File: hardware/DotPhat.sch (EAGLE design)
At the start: 44 parts, among them CN1 1X4-BIG, IC1 CAT24M010TS, J2 RASPBERRYPI-40-PIN-GPIO_PTH, J3 USB-MICROB, U1 ATMEGA328P-MU-QFN32, U2 TMP102, U3 ATSHA204-TSU, U4 W25Q32FV, X3 S4B-ZR

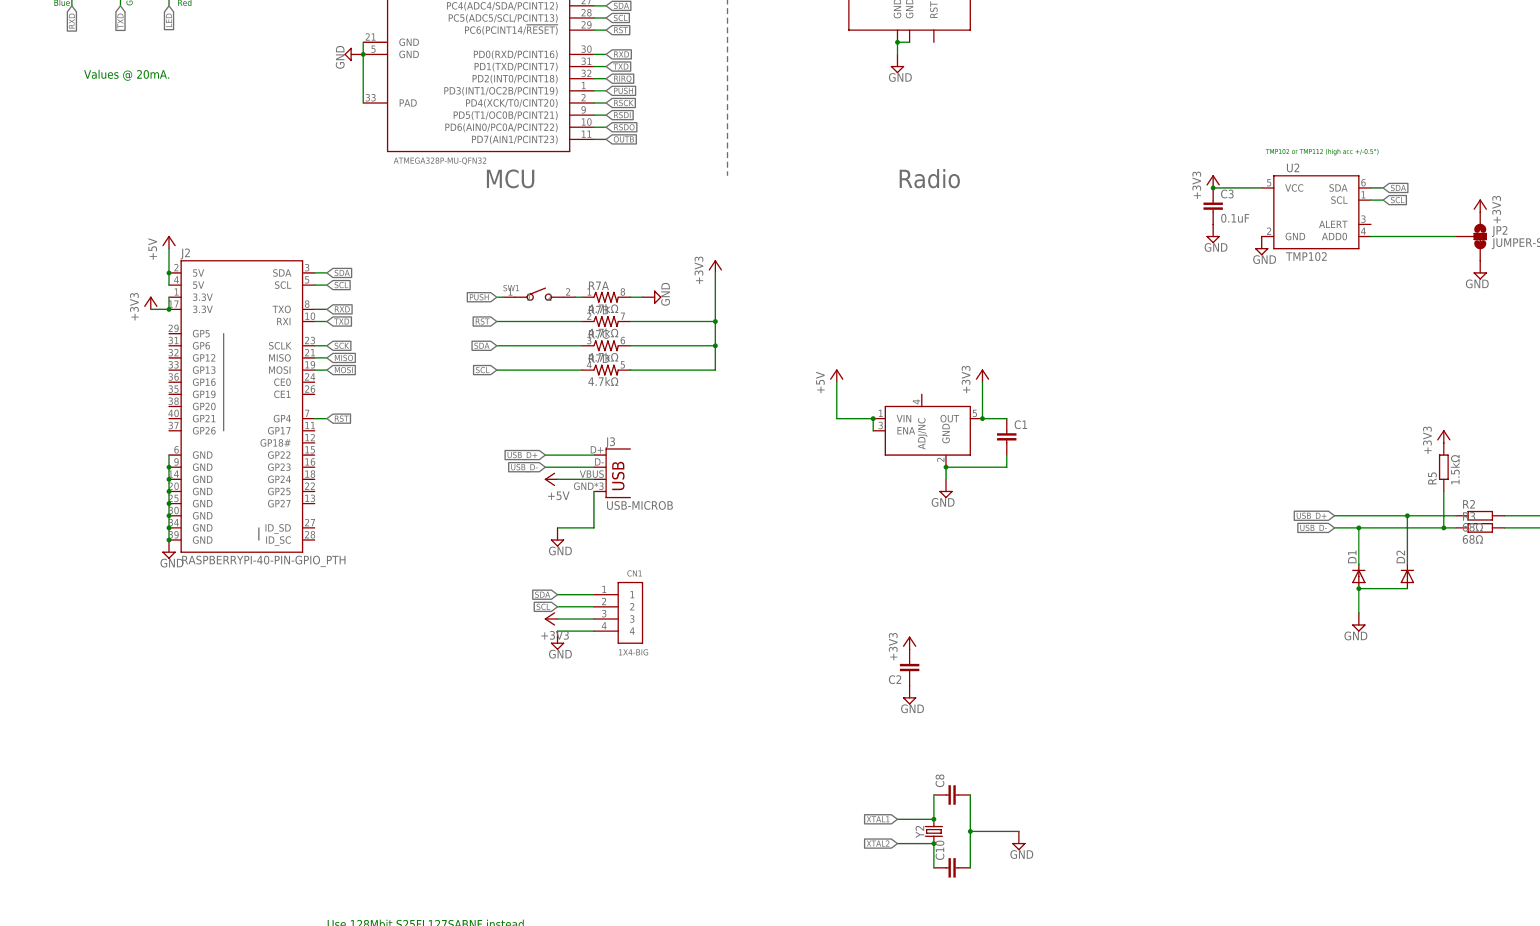
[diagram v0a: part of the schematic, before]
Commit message: Add RTC chip, plug irqs from sensors, flash
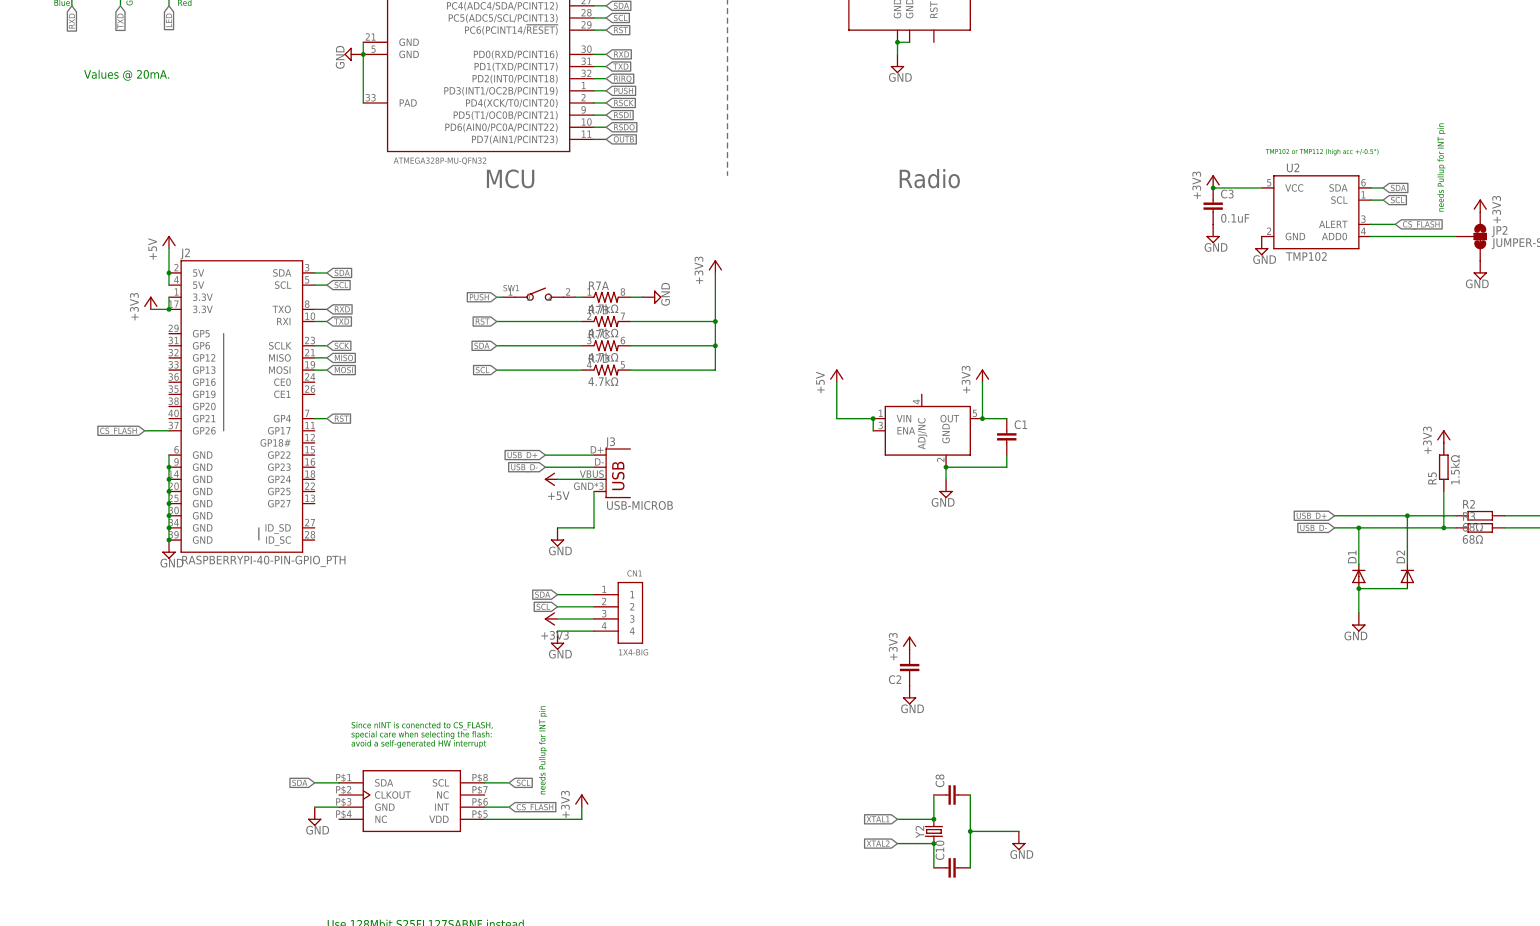
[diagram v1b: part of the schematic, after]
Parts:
- added X2: MC-RTC-RV-4162-C7-I2C, Microcrystal-RTC:MC-RTC-RV-4162-C7-I2C
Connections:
- net +3V3: now also X2.VDD
- net CS_FLASH: now also J2.GP26, U2.ALERT, X2.INT
- net GND: now also X2.GND
- net SCL: now also X2.SCL
- net SDA: now also X2.SDA
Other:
- note added: "Since nINT is conencted to CS_FLASH, special care when selecting the flash: avoid a self-generated HW interrupt"
- note added: "needs Pullup for INT pin"
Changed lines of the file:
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@@
 <part name="R8" library="rcl" deviceset="R-EU_" device="R0603" value="1.5kΩ"/>
 <part name="+3V18" library="supply1" deviceset="+3V3" device=""/>
+<part name="X2" library="Microcrystal-RTC" deviceset="MC-RTC-RV-4162-C7-I2C" device=""/>
+<part name="+3V20" library="supply1" deviceset="+3V3" device=""/>
+<part name="SUPPLY25" library="supply2" deviceset="GND" device=""/>
 </parts>
 <sheets>
@@
 <text x="134.62" y="124.46" size="1.778" layer="91">red</text>
 <text x="20.32" y="-142.24" size="1.778" layer="91">Use 128Mbit S25FL127SABNF instead.</text>
+<text x="25.4" y="-104.14" size="1.27" layer="91">Since nINT is conencted to CS_FLASH,
+special care when selecting the flash:
+avoid a self-generated HW interrupt</text>
+<text x="254" y="7.62" size="1.27" layer="91" rot="R90">needs Pullup for INT pin</text>
+<text x="66.04" y="-114.3" size="1.27" layer="91" rot="R90">needs Pullup for INT pin</text>
 </plain>
 <instances>
@@
 <instance part="R8" gate="G$1" x="25.4" y="-154.94" rot="R90"/>
 <instance part="+3V18" gate="G$1" x="25.4" y="-147.32"/>
+<instance part="X2" gate="G$1" x="38.1" y="-114.3"/>
+<instance part="+3V20" gate="G$1" x="73.66" y="-114.3"/>
+<instance part="SUPPLY25" gate="GND" x="17.78" y="-119.38"/>
 </instances>
 <busses>
@@
 <pinref part="C7" gate="G$1" pin="2"/>
 </segment>
+<segment>
+<pinref part="X2" gate="G$1" pin="GND"/>
+<pinref part="SUPPLY25" gate="GND" pin="GND"/>
+<wire x1="22.86" y1="-116.84" x2="17.78" y2="-116.84" width="0.1524" layer="91"/>
+</segment>
 </net>
 <net name="SDA" class="0">
@@
 <label x="78.74" y="-157.48" size="1.27" layer="95" rot="R180" xref="yes"/>
 <pinref part="IC1" gate="G$1" pin="SDA"/>
+</segment>
+<segment>
+<pinref part="X2" gate="G$1" pin="SDA"/>
+<wire x1="22.86" y1="-111.76" x2="17.78" y2="-111.76" width="0.1524" layer="91"/>
+<label x="17.78" y="-111.76" size="1.27" layer="95" rot="R180" xref="yes"/>
 </segment>
 </net>
@@
 <pinref part="+3V18" gate="G$1" pin="+3V3"/>
 </segment>
+<segment>
+<pinref part="X2" gate="G$1" pin="VDD"/>
+<pinref part="+3V20" gate="G$1" pin="+3V3"/>
+<wire x1="53.34" y1="-119.38" x2="73.66" y2="-119.38" width="0.1524" layer="91"/>
+<wire x1="73.66" y1="-119.38" x2="73.66" y2="-116.84" width="0.1524" layer="91"/>
+</segment>
 </net>
 <net name="ADCENA" class="0">
@@
 <wire x1="81.28" y1="-160.02" x2="78.74" y2="-160.02" width="0.1524" layer="91"/>
 <label x="78.74" y="-160.02" size="1.27" layer="95" rot="R180" xref="yes"/>
+</segment>
+<segment>
+<pinref part="X2" gate="G$1" pin="SCL"/>
+<wire x1="53.34" y1="-111.76" x2="58.42" y2="-111.76" width="0.1524" layer="91"/>
+<label x="58.42" y="-111.76" size="1.27" layer="95" xref="yes"/>
 </segment>
 </net>
@@
 <label x="78.74" y="60.96" size="1.27" layer="95" xref="yes"/>
 </segment>
-</net>
+<segment>
+<pinref part="X2" gate="G$1" pin="INT"/>
+<wire x1="53.34" y1="-116.84" x2="58.42" y2="-116.84" width="0.1524" layer="91"/>
+<label x="58.42" y="-116.84" size="1.27" layer="95" xref="yes"/>
+</segment>
+<segment>
+<label x="243.84" y="5.08" size="1.27" layer="95" xref="yes"/>
+<pinref part="U2" gate="G$1" pin="ALERT"/>
+<wire x1="238.76" y1="5.08" x2="243.84" y2="5.08" width="0.1524" layer="91"/>
+</segment>
+<segment>
+<pinref part="J2" gate="G$1" pin="GP26"/>
+<wire x1="-12.7" y1="-38.1" x2="-17.78" y2="-38.1" width="0.1524" layer="91"/>
+<label x="-17.78" y="-38.1" size="1.27" layer="95" rot="R180" xref="yes"/>
+</segment>
+</net>

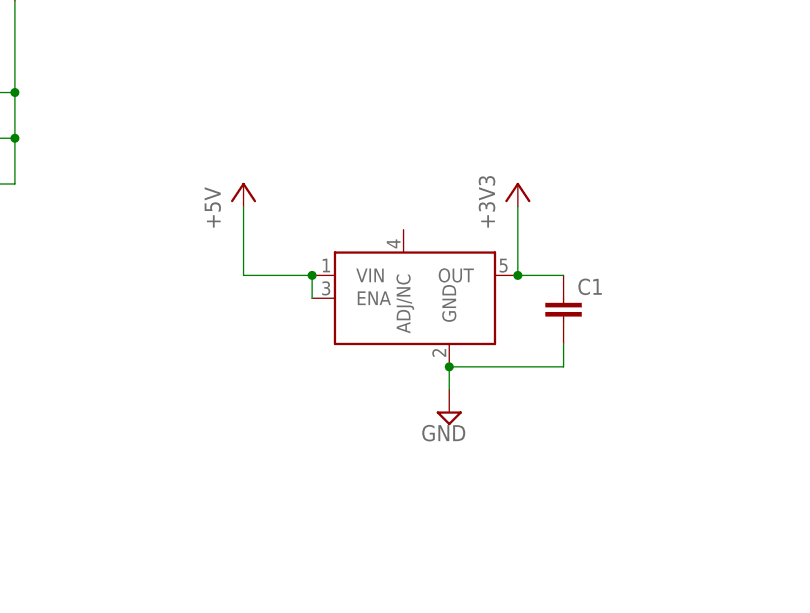
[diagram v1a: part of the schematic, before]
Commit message: Switch to low quiescent LDO
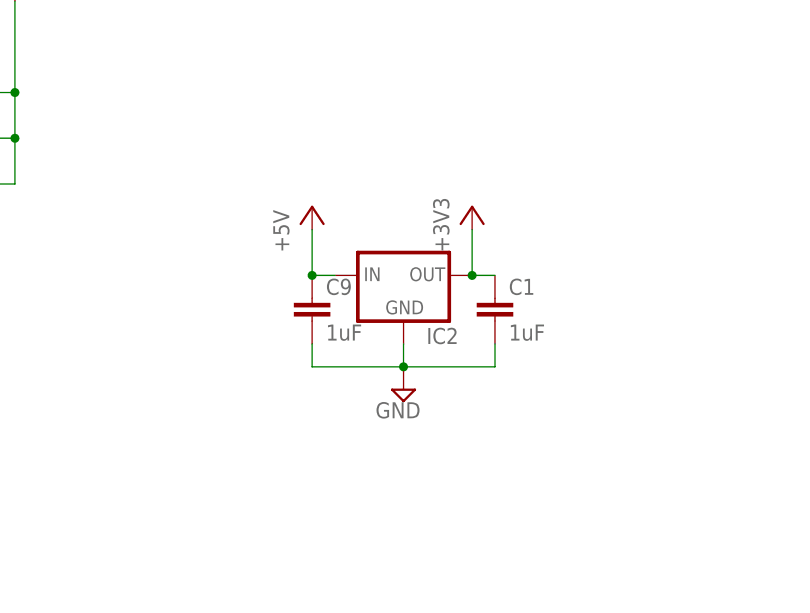
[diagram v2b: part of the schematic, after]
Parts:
- removed U$4: LDCL015, LDCL015:LDCL015
- added C9: 1uF, rcl:C-EUC0603
- added IC2: (no value), MCP1700:MCP1700TT
- C1: value (none) -> 1uF
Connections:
- net +3V3: now also IC2.OUT; no longer U$4.OUT
- net +5V: now also C9.1, IC2.IN; no longer U$4.ENA, U$4.VIN
- net GND: now also C9.2, IC2.GND; no longer U$4.GND
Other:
- moved on the sheet: C1
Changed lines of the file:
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@@
 <part name="R4" library="SparkFun" deviceset="RESISTOR-ARRAY" device="0603-ARV" value="150Ω"/>
 <part name="SUPPLY12" library="supply2" deviceset="GND" device=""/>
-<part name="U$4" library="LDCL015" deviceset="LDCL015" device=""/>
 <part name="SUPPLY27" library="supply2" deviceset="GND" device=""/>
 <part name="+3V19" library="supply1" deviceset="+3V3" device=""/>
 <part name="P+4" library="supply1" deviceset="+5V" device=""/>
-<part name="C1" library="rcl" deviceset="C-EU" device="C0603"/>
+<part name="C1" library="rcl" deviceset="C-EU" device="C0603" value="1uF"/>
 <part name="R1" library="SparkFun" deviceset="RESISTOR-ARRAY" device="0603-ARV"/>
 <part name="U2" library="SparkFun" deviceset="TMP102" device=""/>
@@
 <part name="+3V20" library="supply1" deviceset="+3V3" device=""/>
 <part name="SUPPLY25" library="supply2" deviceset="GND" device=""/>
+<part name="IC2" library="MCP1700" deviceset="MCP1700" device="TT"/>
+<part name="C9" library="rcl" deviceset="C-EU" device="C0603" value="1uF"/>
 </parts>
 <sheets>
@@
 <instance part="R4" gate="D" x="152.4" y="142.24"/>
 <instance part="SUPPLY12" gate="GND" x="160.02" y="152.4" rot="R90"/>
-<instance part="U$4" gate="G$1" x="144.78" y="-38.1"/>
-<instance part="SUPPLY27" gate="GND" x="149.86" y="-50.8" rot="MR0"/>
-<instance part="+3V19" gate="G$1" x="157.48" y="-25.4"/>
-<instance part="P+4" gate="1" x="127" y="-25.4"/>
-<instance part="C1" gate="G$1" x="162.56" y="-38.1"/>
+<instance part="SUPPLY27" gate="GND" x="144.78" y="-48.26" rot="MR0"/>
+<instance part="+3V19" gate="G$1" x="152.4" y="-27.94"/>
+<instance part="P+4" gate="1" x="134.62" y="-27.94"/>
+<instance part="C1" gate="G$1" x="154.94" y="-38.1"/>
 <instance part="R1" gate="A" x="-43.18" y="60.96" rot="R90"/>
 <instance part="R1" gate="B" x="-22.86" y="60.96" rot="R90"/>
@@
 <instance part="+3V20" gate="G$1" x="73.66" y="-114.3"/>
 <instance part="SUPPLY25" gate="GND" x="17.78" y="-119.38"/>
+<instance part="IC2" gate="G$1" x="144.78" y="-35.56"/>
+<instance part="C9" gate="G$1" x="134.62" y="-38.1"/>
 </instances>
 <busses>
@@
 </segment>
 <segment>
-<pinref part="U$4" gate="G$1" pin="GND"/>
-<pinref part="SUPPLY27" gate="GND" pin="GND"/>
-<wire x1="149.86" y1="-48.26" x2="149.86" y2="-45.72" width="0.1524" layer="91"/>
-<pinref part="C1" gate="G$1" pin="2"/>
-<wire x1="149.86" y1="-45.72" x2="162.56" y2="-45.72" width="0.1524" layer="91"/>
-<wire x1="162.56" y1="-45.72" x2="162.56" y2="-43.18" width="0.1524" layer="91"/>
-<junction x="149.86" y="-45.72"/>
-</segment>
-<segment>
 <pinref part="U2" gate="G$1" pin="GND"/>
 <pinref part="SUPPLY15" gate="GND" pin="GND"/>
@@
 <pinref part="SUPPLY25" gate="GND" pin="GND"/>
 <wire x1="22.86" y1="-116.84" x2="17.78" y2="-116.84" width="0.1524" layer="91"/>
+</segment>
+<segment>
+<pinref part="C1" gate="G$1" pin="2"/>
+<wire x1="144.78" y1="-45.72" x2="154.94" y2="-45.72" width="0.1524" layer="91"/>
+<wire x1="154.94" y1="-45.72" x2="154.94" y2="-43.18" width="0.1524" layer="91"/>
+<pinref part="IC2" gate="G$1" pin="GND"/>
+<wire x1="144.78" y1="-43.18" x2="144.78" y2="-45.72" width="0.1524" layer="91"/>
+<pinref part="C9" gate="G$1" pin="2"/>
+<wire x1="134.62" y1="-43.18" x2="134.62" y2="-45.72" width="0.1524" layer="91"/>
+<wire x1="134.62" y1="-45.72" x2="144.78" y2="-45.72" width="0.1524" layer="91"/>
+<junction x="144.78" y="-45.72"/>
+<pinref part="SUPPLY27" gate="GND" pin="GND"/>
 </segment>
 </net>
@@
 </segment>
 <segment>
-<pinref part="U$4" gate="G$1" pin="OUT"/>
 <pinref part="+3V19" gate="G$1" pin="+3V3"/>
-<wire x1="157.48" y1="-27.94" x2="157.48" y2="-35.56" width="0.1524" layer="91"/>
+<wire x1="152.4" y1="-30.48" x2="152.4" y2="-35.56" width="0.1524" layer="91"/>
 <pinref part="C1" gate="G$1" pin="1"/>
-<wire x1="162.56" y1="-35.56" x2="157.48" y2="-35.56" width="0.1524" layer="91"/>
-<junction x="157.48" y="-35.56"/>
+<wire x1="154.94" y1="-35.56" x2="152.4" y2="-35.56" width="0.1524" layer="91"/>
+<pinref part="IC2" gate="G$1" pin="OUT"/>
+<junction x="152.4" y="-35.56"/>
 </segment>
 <segment>
@@
 <segment>
 <pinref part="P+4" gate="1" pin="+5V"/>
-<pinref part="U$4" gate="G$1" pin="VIN"/>
-<wire x1="127" y1="-27.94" x2="127" y2="-35.56" width="0.1524" layer="91"/>
-<wire x1="127" y1="-35.56" x2="134.62" y2="-35.56" width="0.1524" layer="91"/>
-<pinref part="U$4" gate="G$1" pin="ENA"/>
-<wire x1="134.62" y1="-38.1" x2="134.62" y2="-35.56" width="0.1524" layer="91"/>
+<wire x1="134.62" y1="-30.48" x2="134.62" y2="-35.56" width="0.1524" layer="91"/>
+<wire x1="134.62" y1="-35.56" x2="137.16" y2="-35.56" width="0.1524" layer="91"/>
+<pinref part="IC2" gate="G$1" pin="IN"/>
+<pinref part="C9" gate="G$1" pin="1"/>
 <junction x="134.62" y="-35.56"/>
 </segment>

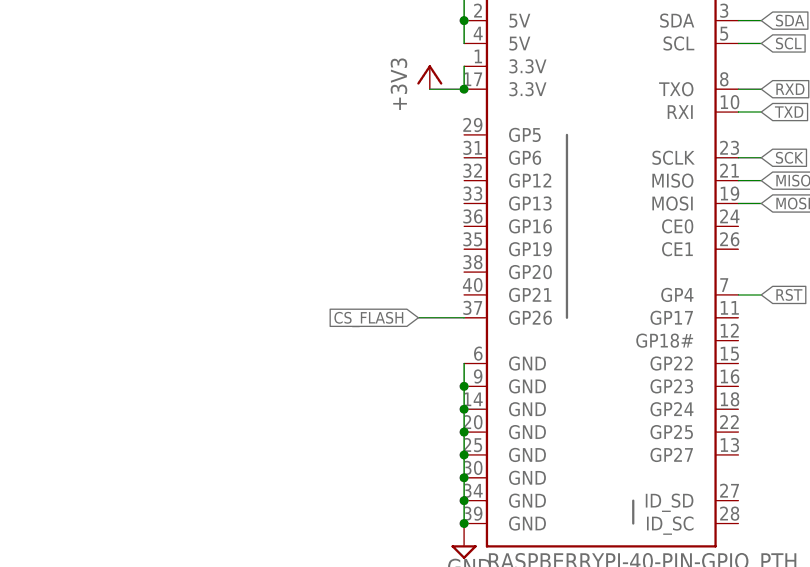
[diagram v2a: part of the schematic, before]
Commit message: Drive OutX from Pi, additionally
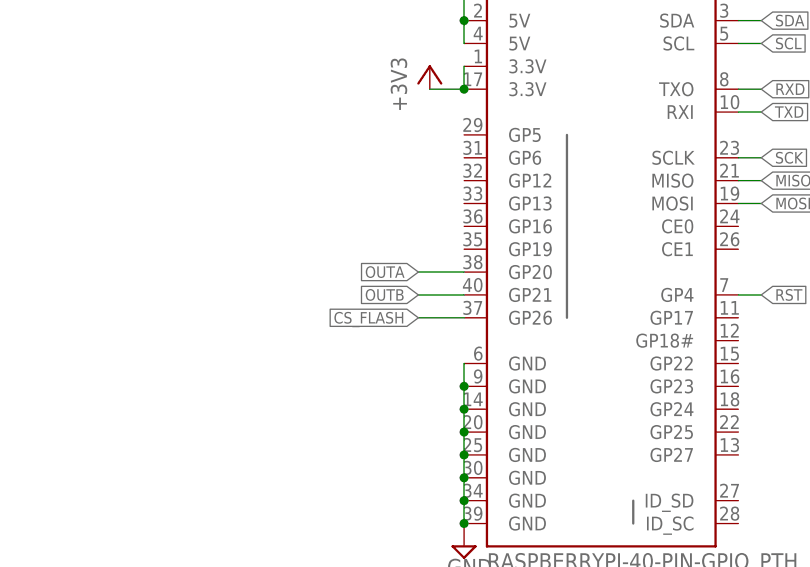
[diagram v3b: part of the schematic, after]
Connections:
- net OUTA: now also J2.GP20
- net OUTB: now also J2.GP21
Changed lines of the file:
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@@
 <label x="78.74" y="22.86" size="1.27" layer="95" xref="yes"/>
+</segment>
+<segment>
+<pinref part="J2" gate="G$1" pin="GP21"/>
+<wire x1="-12.7" y1="-35.56" x2="-17.78" y2="-35.56" width="0.1524" layer="91"/>
+<label x="-17.78" y="-35.56" size="1.27" layer="95" rot="R180" xref="yes"/>
 </segment>
 </net>
@@
 <label x="86.36" y="120.65" size="1.27" layer="95" rot="R180" xref="yes"/>
 </segment>
+<segment>
+<pinref part="J2" gate="G$1" pin="GP20"/>
+<wire x1="-12.7" y1="-33.02" x2="-17.78" y2="-33.02" width="0.1524" layer="91"/>
+<label x="-17.78" y="-33.02" size="1.27" layer="95" rot="R180" xref="yes"/>
+</segment>
 </net>
